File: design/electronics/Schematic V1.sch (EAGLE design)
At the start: 170 parts, among them J1 PJ-202AH, J2 PJ-025, J3 DD50P564GTXLF, J4 DD50P564GTXLF, J5 SAMTEC-TST-105-01-X-DJ, J6 SSW-106-02-TM-S-RA, SW1 TL6330AF200Q, U1 STM32F207VGT6TR, U10 SN65LBC175ADD16-M, U11 MAX7375AXR805+T21-0075D_MXM-M, U12 SN75ALS174ADWRDW20-M, U13 SN75468DRD0016A_M, U14 SN75468DRD0016A_M, U15 ACSL-6400-00TESOIC_6400-00TE-M, U16 ACSL-6400-00TESOIC_6400-00TE-M, U17 SN65LBC175ADD16-M, U18 SN65LBC175ADD16-M, U19 SN65LBC175ADD16-M, U2 LM2678S-5.0/NOPBTS7B-M, U21 RS0104YQTSSOP-14_JRT-M, U22 RS0104YQTSSOP-14_JRT-M, U24 RS0104YQTSSOP-14_JRT-M, U3 CDBC520-GCDBC-G-M, U4 TLV1117LV33DCYR, U5 LM43601PWPRPWP16_TEX-M, U6 RS0104YQTSSOP-14_JRT-M, U7 SN75ALS174ADWRDW20-M, U8 OPA4205APWRTSSOP14_PW_R-PDSO-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

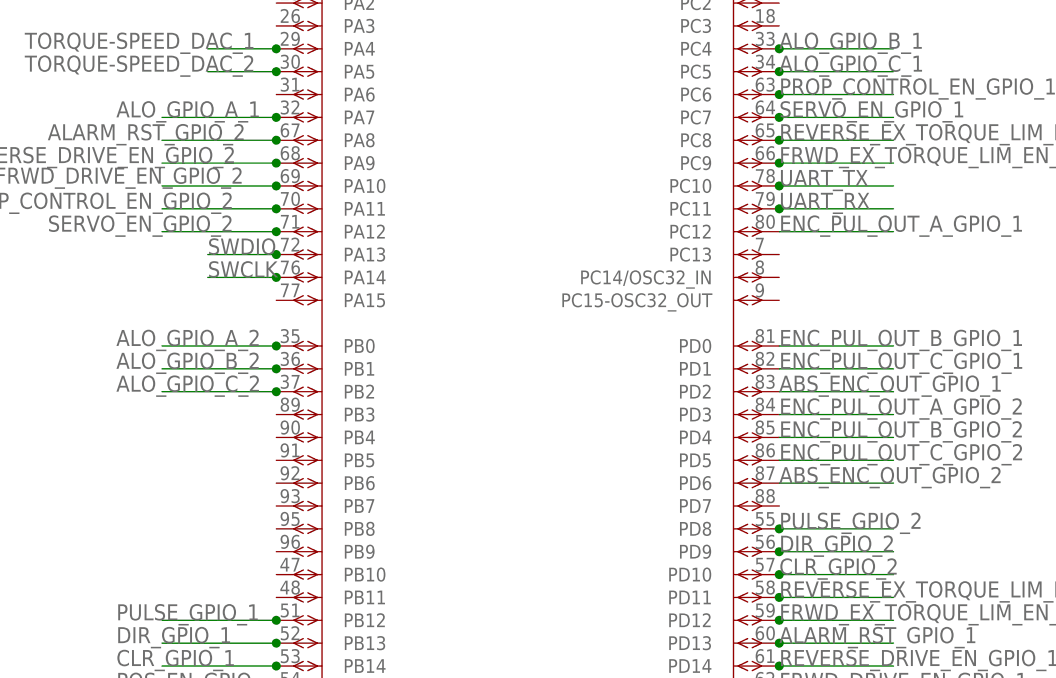
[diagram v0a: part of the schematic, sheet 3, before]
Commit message: Moved UART signals to different pins for routing.
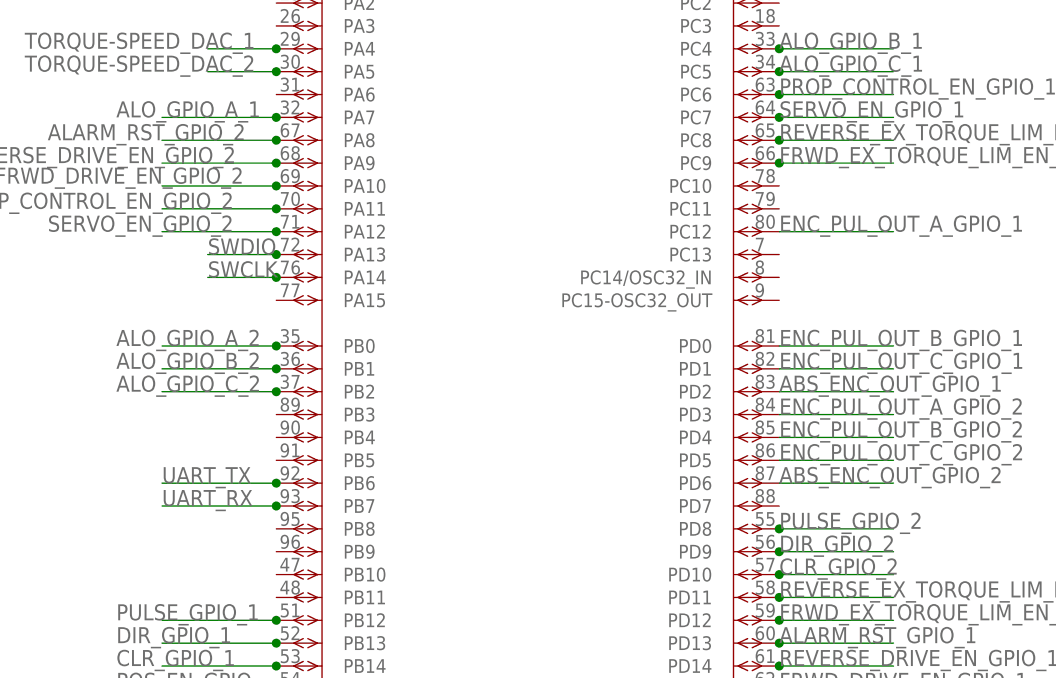
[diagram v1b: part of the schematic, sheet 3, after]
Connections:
- net UART_RX: now also U1A.PB7; no longer U1A.PC11
- net UART_TX: now also U1A.PB6; no longer U1A.PC10
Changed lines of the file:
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@@
 </segment>
 <segment>
-<wire x1="200.66" y1="203.2" x2="213.36" y2="203.2" width="0.1524" layer="91"/>
-<label x="200.66" y="203.2" size="1.778" layer="95"/>
-<pinref part="U1" gate="A" pin="PC11"/>
-<junction x="200.66" y="203.2"/>
+<wire x1="132.08" y1="170.18" x2="144.78" y2="170.18" width="0.1524" layer="91"/>
+<label x="132.08" y="170.18" size="1.778" layer="95"/>
+<pinref part="U1" gate="A" pin="PB7"/>
+<junction x="144.78" y="170.18"/>
 </segment>
 </net>
@@
 </segment>
 <segment>
-<wire x1="200.66" y1="205.74" x2="213.36" y2="205.74" width="0.1524" layer="91"/>
-<label x="200.66" y="205.74" size="1.778" layer="95"/>
-<pinref part="U1" gate="A" pin="PC10"/>
-<junction x="200.66" y="205.74"/>
+<wire x1="132.08" y1="172.72" x2="144.78" y2="172.72" width="0.1524" layer="91"/>
+<label x="132.08" y="172.72" size="1.778" layer="95"/>
+<pinref part="U1" gate="A" pin="PB6"/>
+<junction x="144.78" y="172.72"/>
 </segment>
 </net>

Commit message: Updated schematic, added amazon order purchase
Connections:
- net ABS_ENC_OUT_GPIO_1: now also U1B.PE13; no longer U1A.PD2
- net ABS_ENC_OUT_GPIO_2: no longer U1A.PD6
- net ALARM_RST_AN_1: now also U13.3C; no longer U13.5C
- net ALARM_RST_GPIO_1: now also U13.3B, U1B.PE7; no longer U13.5B, U1A.PD13
- net ALARM_RST_GPIO_2: no longer U1A.PA8
- net ALO_GPIO_A_1: now also U1A.PA6; no longer U1A.PA7
- net ALO_GPIO_A_2: no longer U1A.PB0
- net ALO_GPIO_B_1: now also U1A.PA7; no longer U1A.PC4
- net ALO_GPIO_B_2: no longer U1A.PB1
- net ALO_GPIO_C_1: now also U1A.PC4; no longer U1A.PC5
- net ALO_GPIO_C_2: no longer U1A.PB2
- net CLR_GPIO_2: no longer U1A.PD10
- net DIR_GPIO_2: no longer U1A.PD9
- net ENC_PUL_OUT_A_GPIO_1: now also U1B.PE10; no longer U1A.PC12
- net ENC_PUL_OUT_A_GPIO_2: no longer U1A.PD3
- net ENC_PUL_OUT_B_GPIO_1: now also U1B.PE11; no longer U1A.PD0
- net ENC_PUL_OUT_B_GPIO_2: no longer U1A.PD4
- net ENC_PUL_OUT_C_GPIO_1: now also U1B.PE12; no longer U1A.PD1
- net ENC_PUL_OUT_C_GPIO_2: no longer U1A.PD5
- net FRWD_DRIVE_EN_AN_1: now also U13.5C; no longer U13.3C
- net FRWD_DRIVE_EN_GPIO_1: now also U13.5B, U1A.PB1; no longer U13.3B, U1A.PD15
- net FRWD_DRIVE_EN_GPIO_2: no longer U1A.PA10
- net FRWD_EX_TORQUE_LIM_EN_AN_1: now also U13.2C; no longer U13.6C
- net FRWD_EX_TORQUE_LIM_EN_GPIO_1: now also U13.2B, U1B.PE8; no longer U13.6B, U1A.PD12
- net FRWD_EX_TORQUE_LIM_EN_GPIO_2: no longer U1A.PC9
- net GEN_PURPOSE_OUT_GPIO_A_1: now also U1B.PE14; no longer U1B.PE8
- net GEN_PURPOSE_OUT_GPIO_A_2: no longer U1B.PE12
- net GEN_PURPOSE_OUT_GPIO_B_1: now also U1B.PE15; no longer U1B.PE9
- net GEN_PURPOSE_OUT_GPIO_B_2: no longer U1B.PE13
- net GEN_PURPOSE_OUT_GPIO_C_1: now also U1A.PB10; no longer U1B.PE10
- net GEN_PURPOSE_OUT_GPIO_C_2: no longer U1B.PE14
- net PROP_CONTROL_EN_AN_1: now also U13.6C; no longer U13.2C
- net PROP_CONTROL_EN_GPIO_1: now also U13.6B, U1A.PB0; no longer U13.2B, U1A.PC6
- net PROP_CONTROL_EN_GPIO_2: no longer U1A.PA11
- net PULSE_GPIO_2: no longer U1A.PD8
- net REVERSE_DRIVE_EN_GPIO_1: now also U1A.PB2; no longer U1A.PD14
- net REVERSE_DRIVE_EN_GPIO_2: no longer U1A.PA9
- net REVERSE_EX_TORQUE_LIM_EN_AN_1: now also U13.1C; no longer U13.7C
- net REVERSE_EX_TORQUE_LIM_EN_GPIO_1: now also U13.1B, U1B.PE9; no longer U13.7B, U1A.PD11
- net REVERSE_EX_TORQUE_LIM_EN_GPIO_2: no longer U1A.PC8
- net SERVO_ALARM_OUT_GPIO_1: now also U1A.PB11; no longer U1B.PE11
- net SERVO_ALARM_OUT_GPIO_2: no longer U1B.PE15
- net SERVO_EN_AN_1: now also U13.7C; no longer U13.1C
- net SERVO_EN_GPIO_1: now also U13.7B, U1A.PC5; no longer U13.1B, U1A.PC7
- net SERVO_EN_GPIO_2: no longer U1A.PA12
- net UART_RX: no longer U1A.PB7
- net UART_TX: no longer U1A.PB6

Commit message: Updated Layout more
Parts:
- added R23, R25: 66k, rcl:R-US_R0805
- added R24, R6: 33k, rcl:R-US_R0805
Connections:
- removed net V_ON: R1.2, R2.1, U10.1/2EN, U10.3/4EN, U12.3/42N, U17.1/2EN, U17.3/4EN, U18.1/2EN, U18.3/4EN, U19.1/2EN, U19.3/4EN, U2.ON/~OFF, U7.3/42N
- new net V_ON_14V: R1.2, R2.1, U2.ON/~OFF
- new net V_ON_5V: U10.3/4EN, U12.3/42N, U17.1/2EN, U17.3/4EN, U19.1/2EN, U19.3/4EN
- new net V_ON_5V_1: R23.2, R6.1, U10.1/2EN, U18.1/2EN, U18.3/4EN
- new net V_ON_5V_2: R24.1, R25.2, U7.3/42N
- net +5V: now also R24.2, R6.2
- net S_GND: now also R23.1, R25.1
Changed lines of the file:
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@@
 <part name="C14" library="SparkFun-Capacitors" deviceset="4.7UF" device="-0805-50V-(10%)" value="10uF"/>
 <part name="R1" library="rcl" library_urn="urn:adsk.eagle:library:334" deviceset="R-US_" device="R0805" package3d_urn="urn:adsk.eagle:package:23553/2" value="25k"/>
+<part name="R6" library="rcl" library_urn="urn:adsk.eagle:library:334" deviceset="R-US_" device="R0805" package3d_urn="urn:adsk.eagle:package:23553/2" value="33k"/>
+<part name="R23" library="rcl" library_urn="urn:adsk.eagle:library:334" deviceset="R-US_" device="R0805" package3d_urn="urn:adsk.eagle:package:23553/2" value="66k"/>
+<part name="R24" library="rcl" library_urn="urn:adsk.eagle:library:334" deviceset="R-US_" device="R0805" package3d_urn="urn:adsk.eagle:package:23553/2" value="33k"/>
+<part name="R25" library="rcl" library_urn="urn:adsk.eagle:library:334" deviceset="R-US_" device="R0805" package3d_urn="urn:adsk.eagle:package:23553/2" value="66k"/>
 </parts>
 <sheets>
@@
 <attribute name="VALUE" x="143.51" y="231.902" size="1.778" layer="96" rot="R180"/>
 </instance>
+<instance part="R6" gate="G$1" x="124.46" y="220.98" smashed="yes" rot="R180">
+<attribute name="NAME" x="128.27" y="219.4814" size="1.778" layer="95" rot="R180"/>
+<attribute name="VALUE" x="128.27" y="224.282" size="1.778" layer="96" rot="R180"/>
+</instance>
+<instance part="R23" gate="G$1" x="139.7" y="220.98" smashed="yes" rot="R180">
+<attribute name="NAME" x="143.51" y="219.4814" size="1.778" layer="95" rot="R180"/>
+<attribute name="VALUE" x="143.51" y="224.282" size="1.778" layer="96" rot="R180"/>
+</instance>
+<instance part="R24" gate="G$1" x="124.46" y="213.36" smashed="yes" rot="R180">
+<attribute name="NAME" x="128.27" y="211.8614" size="1.778" layer="95" rot="R180"/>
+<attribute name="VALUE" x="128.27" y="216.662" size="1.778" layer="96" rot="R180"/>
+</instance>
+<instance part="R25" gate="G$1" x="139.7" y="213.36" smashed="yes" rot="R180">
+<attribute name="NAME" x="143.51" y="211.8614" size="1.778" layer="95" rot="R180"/>
+<attribute name="VALUE" x="143.51" y="216.662" size="1.778" layer="96" rot="R180"/>
+</instance>
 </instances>
 <busses>
@@
 <label x="254" y="144.78" size="1.778" layer="95"/>
 </segment>
+<segment>
+<wire x1="111.76" y1="220.98" x2="119.38" y2="220.98" width="0.1524" layer="91"/>
+<label x="111.76" y="220.98" size="1.778" layer="95"/>
+<pinref part="R6" gate="G$1" pin="2"/>
+<junction x="119.38" y="220.98"/>
+</segment>
+<segment>
+<wire x1="111.76" y1="213.36" x2="119.38" y2="213.36" width="0.1524" layer="91"/>
+<label x="111.76" y="213.36" size="1.778" layer="95"/>
+<pinref part="R24" gate="G$1" pin="2"/>
+<junction x="119.38" y="213.36"/>
+</segment>
 </net>
 <net name="N$2" class="0">
@@
 </segment>
 </net>
-<net name="V_ON" class="0">
-<segment>
-<pinref part="U2" gate="A" pin="ON/~OFF"/>
-<wire x1="355.6" y1="142.24" x2="360.68" y2="142.24" width="0.1524" layer="91"/>
-<label x="355.6" y="142.24" size="1.778" layer="95"/>
-</segment>
-<segment>
-<wire x1="129.54" y1="228.6" x2="134.62" y2="228.6" width="0.1524" layer="91"/>
-<label x="129.54" y="228.6" size="1.778" layer="95"/>
-<pinref part="R2" gate="G$1" pin="1"/>
-<junction x="129.54" y="228.6"/>
-<pinref part="R1" gate="G$1" pin="2"/>
-</segment>
-</net>
 <net name="S_GND" class="0">
 <segment>
@@
 <label x="116.84" y="12.7" size="1.778" layer="95"/>
 </segment>
+<segment>
+<wire x1="144.78" y1="220.98" x2="152.4" y2="220.98" width="0.1524" layer="91"/>
+<label x="147.32" y="220.98" size="1.778" layer="95"/>
+<pinref part="R23" gate="G$1" pin="1"/>
+</segment>
+<segment>
+<wire x1="144.78" y1="213.36" x2="152.4" y2="213.36" width="0.1524" layer="91"/>
+<label x="147.32" y="213.36" size="1.778" layer="95"/>
+<pinref part="R25" gate="G$1" pin="1"/>
+</segment>
 </net>
 <net name="N$4" class="0">
@@
 </segment>
 </net>
+<net name="V_ON_14V" class="0">
+<segment>
+<wire x1="129.54" y1="228.6" x2="134.62" y2="228.6" width="0.1524" layer="91"/>
+<label x="129.54" y="228.6" size="1.778" layer="95"/>
+<pinref part="R2" gate="G$1" pin="1"/>
+<junction x="129.54" y="228.6"/>
+<pinref part="R1" gate="G$1" pin="2"/>
+</segment>
+<segment>
+<pinref part="U2" gate="A" pin="ON/~OFF"/>
+<wire x1="355.6" y1="142.24" x2="360.68" y2="142.24" width="0.1524" layer="91"/>
+<label x="355.6" y="142.24" size="1.778" layer="95"/>
+</segment>
+</net>
+<net name="V_ON_5V_1" class="0">
+<segment>
+<wire x1="129.54" y1="220.98" x2="134.62" y2="220.98" width="0.1524" layer="91"/>
+<label x="129.54" y="220.98" size="1.778" layer="95"/>
+<pinref part="R6" gate="G$1" pin="1"/>
+<junction x="129.54" y="220.98"/>
+<pinref part="R23" gate="G$1" pin="2"/>
+</segment>
+</net>
+<net name="V_ON_5V_2" class="0">
+<segment>
+<wire x1="129.54" y1="213.36" x2="134.62" y2="213.36" width="0.1524" layer="91"/>
+<label x="129.54" y="213.36" size="1.778" layer="95"/>
+<pinref part="R24" gate="G$1" pin="1"/>
+<junction x="129.54" y="213.36"/>
+<pinref part="R25" gate="G$1" pin="2"/>
+</segment>
+</net>
 </nets>
 </sheet>
@@
 </segment>
 </net>
-<net name="V_ON" class="0">
-<segment>
-<wire x1="454.66" y1="203.2" x2="439.42" y2="203.2" width="0.1524" layer="91"/>
-<pinref part="U10" gate="A" pin="1/2EN"/>
-<label x="434.34" y="203.2" size="1.778" layer="95"/>
-</segment>
-<segment>
-<wire x1="523.24" y1="200.66" x2="515.62" y2="200.66" width="0.1524" layer="91"/>
-<pinref part="U10" gate="A" pin="3/4EN"/>
-<label x="515.62" y="200.66" size="1.778" layer="95"/>
-</segment>
-<segment>
-<wire x1="454.66" y1="160.02" x2="439.42" y2="160.02" width="0.1524" layer="91"/>
-<pinref part="U17" gate="A" pin="1/2EN"/>
-<label x="434.34" y="160.02" size="1.778" layer="95"/>
-</segment>
-<segment>
-<wire x1="523.24" y1="157.48" x2="515.62" y2="157.48" width="0.1524" layer="91"/>
-<pinref part="U17" gate="A" pin="3/4EN"/>
-<label x="515.62" y="157.48" size="1.778" layer="95"/>
-</segment>
-<segment>
-<pinref part="U18" gate="A" pin="1/2EN"/>
-<wire x1="457.2" y1="96.52" x2="447.04" y2="96.52" width="0.1524" layer="91"/>
-<label x="447.04" y="96.52" size="1.778" layer="95"/>
-<junction x="457.2" y="96.52"/>
-</segment>
-<segment>
-<wire x1="518.16" y1="93.98" x2="525.78" y2="93.98" width="0.1524" layer="91"/>
-<label x="520.7" y="93.98" size="1.778" layer="95"/>
-<pinref part="U18" gate="A" pin="3/4EN"/>
-</segment>
-<segment>
-<pinref part="U19" gate="A" pin="1/2EN"/>
-<wire x1="457.2" y1="38.1" x2="447.04" y2="38.1" width="0.1524" layer="91"/>
-<label x="447.04" y="38.1" size="1.778" layer="95"/>
-<junction x="457.2" y="38.1"/>
-</segment>
-<segment>
-<wire x1="518.16" y1="35.56" x2="525.78" y2="35.56" width="0.1524" layer="91"/>
-<label x="520.7" y="35.56" size="1.778" layer="95"/>
-<pinref part="U19" gate="A" pin="3/4EN"/>
-</segment>
-<segment>
-<pinref part="U12" gate="A" pin="3/42N"/>
-<wire x1="101.6" y1="157.48" x2="109.22" y2="157.48" width="0.1524" layer="91"/>
-<label x="101.6" y="157.48" size="1.778" layer="95"/>
-</segment>
-<segment>
-<pinref part="U7" gate="A" pin="3/42N"/>
-<wire x1="104.14" y1="198.12" x2="111.76" y2="198.12" width="0.1524" layer="91"/>
-<label x="104.14" y="198.12" size="1.778" layer="95"/>
-</segment>
-</net>
 <net name="GEN_PURPOSE_OUT_HI_A_1" class="0">
 <segment>
@@
 </segment>
 </net>
+<net name="V_ON_5V" class="0">
+<segment>
+<wire x1="523.24" y1="200.66" x2="515.62" y2="200.66" width="0.1524" layer="91"/>
+<pinref part="U10" gate="A" pin="3/4EN"/>
+<label x="515.62" y="200.66" size="1.778" layer="95"/>
+</segment>
+<segment>
+<wire x1="523.24" y1="157.48" x2="515.62" y2="157.48" width="0.1524" layer="91"/>
+<pinref part="U17" gate="A" pin="3/4EN"/>
+<label x="515.62" y="157.48" size="1.778" layer="95"/>
+</segment>
+<segment>
+<wire x1="454.66" y1="160.02" x2="439.42" y2="160.02" width="0.1524" layer="91"/>
+<pinref part="U17" gate="A" pin="1/2EN"/>
+<label x="434.34" y="160.02" size="1.778" layer="95"/>
+</segment>
+<segment>
+<wire x1="518.16" y1="35.56" x2="525.78" y2="35.56" width="0.1524" layer="91"/>
+<label x="520.7" y="35.56" size="1.778" layer="95"/>
+<pinref part="U19" gate="A" pin="3/4EN"/>
+</segment>
+<segment>
+<pinref part="U19" gate="A" pin="1/2EN"/>
+<wire x1="457.2" y1="38.1" x2="447.04" y2="38.1" width="0.1524" layer="91"/>
+<label x="447.04" y="38.1" size="1.778" layer="95"/>
+<junction x="457.2" y="38.1"/>
+</segment>
+<segment>
+<pinref part="U12" gate="A" pin="3/42N"/>
+<wire x1="101.6" y1="157.48" x2="109.22" y2="157.48" width="0.1524" layer="91"/>
+<label x="101.6" y="157.48" size="1.778" layer="95"/>
+</segment>
+</net>
+<net name="V_ON_5V_1" class="0">
+<segment>
+<wire x1="454.66" y1="203.2" x2="439.42" y2="203.2" width="0.1524" layer="91"/>
+<pinref part="U10" gate="A" pin="1/2EN"/>
+<label x="434.34" y="203.2" size="1.778" layer="95"/>
+</segment>
+<segment>
+<pinref part="U18" gate="A" pin="1/2EN"/>
+<wire x1="457.2" y1="96.52" x2="447.04" y2="96.52" width="0.1524" layer="91"/>
+<label x="447.04" y="96.52" size="1.778" layer="95"/>
+<junction x="457.2" y="96.52"/>
+</segment>
+<segment>
+<wire x1="518.16" y1="93.98" x2="525.78" y2="93.98" width="0.1524" layer="91"/>
+<label x="520.7" y="93.98" size="1.778" layer="95"/>
+<pinref part="U18" gate="A" pin="3/4EN"/>
+</segment>
+</net>
+<net name="V_ON_5V_2" class="0">
+<segment>
+<pinref part="U7" gate="A" pin="3/42N"/>
+<wire x1="104.14" y1="198.12" x2="111.76" y2="198.12" width="0.1524" layer="91"/>
+<label x="104.14" y="198.12" size="1.778" layer="95"/>
+</segment>
+</net>

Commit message: Layout almost done
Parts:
- added R26, R71, R73: 33k, rcl:R-US_R0805
- added R70, R72, R74: 66k, rcl:R-US_R0805
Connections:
- new net V_ON_5V_3: R26.1, R70.2, U10.1/2EN, U10.3/4EN
- new net V_ON_5V_4: R71.1, R72.2, U17.1/2EN, U17.3/4EN
- new net V_ON_5V_5: R73.1, R74.2, U19.1/2EN, U19.3/4EN
- net +5V: now also R26.2, R71.2, R73.2
- net ABS_ENC_OUT_GPIO_2: now also U1A.PB4
- net ALARM_RST_GPIO_2: now also U1A.PD3
- net ALO_GPIO_A_2: now also U1A.PA15
- net ALO_GPIO_B_2: now also U1A.PC10
- net ALO_GPIO_C_2: now also U1A.PC11
- net CLR_GPIO_1: now also U1A.PB15; no longer U1A.PB14
- net CLR_GPIO_2: now also U1A.PA10
- net DIR_GPIO_1: now also U1A.PB14; no longer U1A.PB13
- net DIR_GPIO_2: now also U1A.PA12
- net ENC_PUL_OUT_A_GPIO_2: now also U1A.PD6
- net ENC_PUL_OUT_B_GPIO_2: now also U1A.PD7
- net ENC_PUL_OUT_C_GPIO_2: now also U1A.PB3
- net FRWD_DRIVE_EN_GPIO_2: now also U1A.PD1
- net FRWD_EX_TORQUE_LIM_EN_GPIO_2: now also U1A.PD4
- net GEN_PURPOSE_OUT_GPIO_A_2: now also U1A.PB5
- net GEN_PURPOSE_OUT_GPIO_B_2: now also U1A.PB6
- net GEN_PURPOSE_OUT_GPIO_C_2: now also U1A.PB7
- net POS_EN_GPIO: now also U1A.PD8; no longer U1A.PB15
- net PROP_CONTROL_EN_GPIO_2: now also U1A.PD0
- net PULSE_GPIO_1: now also U1A.PB13; no longer U1A.PB12
- net PULSE_GPIO_2: now also U1A.PA11
- net REVERSE_DRIVE_EN_GPIO_2: now also U1A.PD2
- net REVERSE_EX_TORQUE_LIM_EN_GPIO_2: now also U1A.PD5
- net SERVO_ALARM_OUT_GPIO_2: now also U1A.PB8
- net SERVO_EN_GPIO_2: now also U1A.PC12
- net S_GND: now also R70.1, R72.1, R74.1
- net UART_RX: now also U1A.PC7
- net UART_TX: now also U1A.PC6
- net V_ON_5V: no longer U10.3/4EN, U17.1/2EN, U17.3/4EN, U19.1/2EN, U19.3/4EN
- net V_ON_5V_1: no longer U10.1/2EN
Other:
- moved on the sheet: R1, R2, R23, R24, R25, R6

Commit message: Yay it's hooked up
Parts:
- added R75: 33k, rcl:R-US_R0805
- added R76: 66k, rcl:R-US_R0805
- renumbered U10 to LINE_RECEIVER, U13 to NPN, U15 to OPTOCOUPLER, U21 to LEVEL_SHIFTER
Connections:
- removed net V_ON_5V: U12.3/42N
- new net V_ON_5V_6: R75.1, R76.2, U12.3/42N
- net +5V: now also R75.2
- net S_GND: now also R76.1

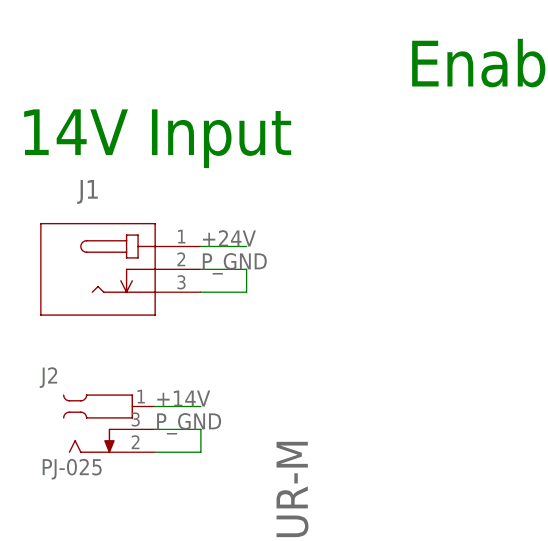
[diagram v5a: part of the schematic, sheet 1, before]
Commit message: Updated part library of barrel jack + stretched polygons
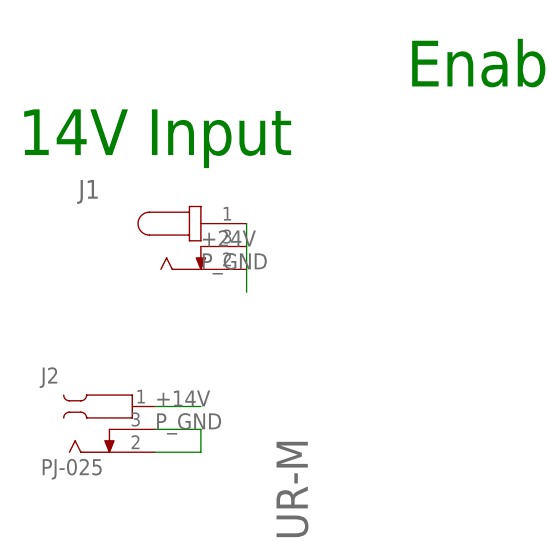
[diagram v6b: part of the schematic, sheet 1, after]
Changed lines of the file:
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@@
 <attribute name="VALUE" x="130.556" y="144.399" size="1.778" layer="96" font="vector" rot="R180"/>
 </instance>
-<instance part="J1" gate="A" x="45.72" y="231.14" smashed="yes">
+<instance part="J1" gate="G$1" x="45.72" y="231.14" smashed="yes">
 <attribute name="NAME" x="32.1056" y="236.4486" size="2.0828" layer="95" ratio="6" rot="SR0"/>
 </instance>
@@
 </segment>
 <segment>
-<pinref part="J1" gate="A" pin="2"/>
-<wire x1="45.72" y1="228.6" x2="50.8" y2="228.6" width="0.1524" layer="91"/>
-<pinref part="J1" gate="A" pin="3"/>
+<pinref part="J1" gate="G$1" pin="2"/>
+<pinref part="J1" gate="G$1" pin="3"/>
 <wire x1="50.8" y1="228.6" x2="50.8" y2="226.06" width="0.1524" layer="91"/>
-<wire x1="50.8" y1="226.06" x2="45.72" y2="226.06" width="0.1524" layer="91"/>
+<wire x1="50.8" y1="228.6" x2="50.8" y2="231.14" width="0.1524" layer="91"/>
 <label x="45.72" y="228.6" size="1.778" layer="95"/>
 </segment>
@@
 <net name="+24V" class="0">
 <segment>
-<pinref part="J1" gate="A" pin="1"/>
-<wire x1="45.72" y1="231.14" x2="50.8" y2="231.14" width="0.1524" layer="91"/>
+<pinref part="J1" gate="G$1" pin="1"/>
+<wire x1="50.8" y1="233.68" x2="50.8" y2="231.14" width="0.1524" layer="91"/>
 <label x="45.72" y="231.14" size="1.778" layer="95"/>
 </segment>

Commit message: Finished PCB
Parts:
- renumbered C2 to 180UF, C3 to 330UF_C3, C7 to 0.01UF_C7, J2 to 14_JACK, J5 to ST-LINK_CONNECTOR, J6 to UART_CONNECTOR, L1 to 10UH_L1, LEVEL_SHIFTER to LEVEL_SHIFTER2, LINE_RECEIVER to LINE_RECEIVER1, SW1 to BUTTON, U1 to STM32F2, U11 to OSCILLATOR, U12 to LINE_DRIVER2, U14 to NPN2, U16 to OPTOCOUPLER2, U17 to LINE_RECEIVER3, U18 to LINE_RECEIVER2, U19 to LINE_RECEIVER4, U2 to 5V, U22 to LEVEL_SHIFTER1, U24 to LEVEL_SHIFTER3, U3 to DIODE, U4 to LDO, U5 to -15V, U6 to LEVEL_SHIFTER4, U7 to LINE_DRIVER1, U8 to OP_AMP
